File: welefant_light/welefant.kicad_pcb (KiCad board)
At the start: 2 copper layers, 80 x 90 mm, 75 parts, among them J1 Conn_01x02, J2 Conn_02x8_Odd_Even, J3 Conn_02x11_Odd_Even, Q1 AO3401A, Q2 AO3401A, Q3 AO3401A, SW1 RESET, SW2 RESET, SW3 BOOT, U1 NCP167BMX330TBG, U2 Audio Jack PJ-324, U3 GSA4737H12-F26-6P, U4 TP4056, U5 welefant, U6 ESP32-S3-WROOM-1(N16R2)

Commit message: blubb
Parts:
- removed R11: 2.4K, easyeda2kicad:R0603
- added R18: 10K, easyeda2kicad:R0603, F.Cu at (42.0, 50.4)
- added R19: 330, easyeda2kicad:R0603, F.Cu at (50.2, 80.1)
- BT1: value Battery_Cell -> Battery
- D4: value SS34 -> 1N5819WS; footprint easyeda2kicad:SMA_L4.3-W2.6-LS5.2-RD -> Diode_SMD:D_SOD-323
- J1: footprint Connector_JST:JST_PH_B2B-PH-SM4-TB_1x02-1MP_P2.00mm_Vertical -> Connector_JST:JST_PH_B2B-PH-K_1x02_P2.00mm_Vertical
- J2, J3: footprint Connector_PinHeader_2.54mm:PinHeader_2x08_P2.54mm_Vertical_SMD -> hacrafu:PinHeader_2x08_P2.54mm_Vertical_SMD_handsolder
- SW1: value RESET -> DPDT; footprint easyeda2kicad:SW-SMD_4P-L5.1-W5.1-P3.70-LS6.5-TL-2 -> hacrafu:Switch_MSS22D18
- U1: footprint easyeda2kicad:XDFN-4_L1.0-W1.0-P0.65-BL-EP -> hacrafu:XDFN-4
- moved D4 111.2 mm to (96.6, 95.8), turned to 180 degrees
- moved R10 86.2 mm to (55.9, 73.6), turned to -90 degrees
- moved SW1 79.8 mm to (45.9, 86.9), turned to -90 degrees
- moved D2 74.6 mm to (57.8, 59.0), turned to 90 degrees
- moved D1 74.0 mm to (60.0, 59.0), turned to 90 degrees
- moved C8 71.4 mm to (51.5, 74.2), turned to 90 degrees
- moved CLED1 69.8 mm to (50.2, 78.6), turned to 180 degrees
- moved J1 64.5 mm to (46.4, 96.3)
- moved Q2 63.7 mm to (57.9, 78.0), turned to -90 degrees
- moved U4 63.2 mm to (47.5, 74.1), turned to 180 degrees
- moved C11 62.0 mm to (34.0, 46.6), turned to 90 degrees
- moved R9 60.7 mm to (54.6, 79.2), turned to 180 degrees
- moved SW3 57.9 mm to (94.4, 67.0)
- moved D3 57.7 mm to (53.9, 74.4), turned to 90 degrees
- moved C7 56.3 mm to (74.0, 65.9), turned to -90 degrees
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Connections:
- C11 pad 1: Net-(SW2-B) -> /RESET
- C11 pad 2: Net-(SW2-D) -> GND
- C3 pad 1: (no net) -> GND
- C3 pad 2: (no net) -> /V33
- C6 pad 1: (no net) -> /VBUS
- C6 pad 2: (no net) -> GND
- Q1 pad 1: (no net) -> Net-(Q1-G)
- Q1 pad 2: (no net) -> /V33
- Q1 pad 3: (no net) -> /VEXT
- R1 pad 1: (no net) -> /V33
- R1 pad 2: (no net) -> /VEXT_EN
- R17 pad 2: Net-(SW2-B) -> /RESET
- R3 pad 1: (no net) -> Net-(Q1-G)
- R3 pad 2: (no net) -> /VEXT_EN
- SW1 pad 2: Net-(SW1-B) -> unconnected-(SW1-AB1-Pad2)
- SW1 pad 3: /GND -> unconnected-(SW1-B1-Pad3)
- SW1 pad 4: Net-(SW1-D) -> unconnected-(SW1-A2-Pad4)
- SW2 pad 1: unconnected-(SW2-A-Pad1) -> /RESET
- SW2 pad 2: Net-(SW2-B) -> /RESET
- SW2 pad 4: Net-(SW2-D) -> GND
- SW3 pad 1: Net-(SW3-A) -> /IO0
- SW3 pad 2: unconnected-(SW3-B-Pad2) -> /IO0
- SW3 pad 3: unconnected-(SW3-C-Pad3) -> GND
- U1 pad 1: (no net) -> /V33
- U1 pad 2: (no net) -> GND
- U1 pad 3: (no net) -> /VBUS
- U1 pad 4: (no net) -> /VBUS
- U1 pad 5: (no net) -> GND
- U4 pad 9: unconnected-(U4-EP-Pad9) -> GND
- U6 pad 27: Net-(SW3-A) -> /IO0
- U6 pad 3: Net-(SW2-B) -> /RESET
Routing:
- net /VEXT: track 0.00 -> 242.7 mm, vias 0 -> 4
- net /V33: track 0.00 -> 131.2 mm, vias 0 -> 2
- net /TOUCH_T4: track 0.00 -> 115.4 mm, vias 0 -> 3
- net /TOUCH_T1: track 0.00 -> 114.3 mm, vias 0 -> 3
- net /TOUCH_T6: track 0.00 -> 113.0 mm, vias 0 -> 5
- net /TOUCH_T2: track 0.00 -> 108.8 mm, vias 0 -> 3
- net /TOUCH_T5: track 0.00 -> 106.5 mm, vias 0 -> 5
- net /TOUCH_T3: track 0.00 -> 100.3 mm, vias 0 -> 3
- net /USB_DN: track 0.00 -> 97.2 mm
- net /AUDIO_PWM_L: track 0.00 -> 93.6 mm, vias 0 -> 2
- net /USB_DP: track 0.00 -> 88.0 mm
- net /AUDIO_PWM_R: track 0.00 -> 82.2 mm, vias 0 -> 2
- net /V5: track 0.00 -> 81.9 mm, vias 0 -> 2
- net /JACK_SENS: track 0.00 -> 81.0 mm, vias 0 -> 1
- net /LED_MATRIX: track 0.00 -> 70.7 mm, vias 0 -> 8
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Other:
- outline, holes or cut-outs redrawn

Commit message: stand
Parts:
- BT1: footprint hacrafu:LiPo_Recycled -> hacrafu:LiPo_Recycled_welefant
- J3: value Conn_02x11_Odd_Even -> Conn_02x6_Odd_Even; footprint hacrafu:PinHeader_2x08_P2.54mm_Vertical_SMD_handsolder -> hacrafu:PinHeader_2x06_P2.54mm_Vertical_SMD_handsolder
- moved J3 5.09 mm to (94.0, 45.9)
- moved C10 0.22 mm to (43.5, 77.0)
- moved R19 0.08 mm to (50.2, 80.2)
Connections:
- J3 pad 10: /IO36 -> /IO40
- J3 pad 11: /IO37 -> /IO41
- J3 pad 12: /IO38 -> /IO42
- J3 pad 5: /TOUCH_T4 -> /IO35
- J3 pad 6: /TOUCH_T5 -> /IO36
- J3 pad 7: /TOUCH_T6 -> /IO37
- J3 pad 8: /IO21 -> /IO38
- J3 pad 9: /IO35 -> /IO39
- U6 pad 23: /IO21 -> unconnected-(U6-IO21-Pad23)
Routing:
- net GND: track 7.59 -> 61.9 mm, vias 57 -> 100
- net /TOUCH_T4: track 115.4 -> 84.2 mm
- net /TOUCH_T6: track 113.0 -> 82.0 mm, vias 5 -> 3
- net /IO21: track 29.1 -> 0.00 mm, vias 2 -> 0
- net /TOUCH_T5: track 106.5 -> 80.4 mm, vias 5 -> 3
- net /V5: track 81.9 -> 96.3 mm, vias 2 -> 5
- net /LED_MATRIX: track 70.7 -> 84.9 mm, vias 8 -> 6
- net /V33: track 131.2 -> 140.3 mm
- net /TOUCH_T1: track 114.3 -> 105.9 mm
- net /VEXT: track 242.7 -> 248.1 mm
- net /D2_LED: track 32.2 -> 37.4 mm
- net /TOUCH_T2: track 108.8 -> 104.4 mm
- net /TOUCH_ER: track 37.5 -> 41.3 mm, vias 1 -> 3
- net /VBUS: track 60.4 -> 56.8 mm, vias 4 -> 2
- net /VEXT_EN: track 52.0 -> 55.5 mm
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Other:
- board text added: "35"
- board text added: "36"
- board text added: "37"
- board text added: "38"
- board text added: "39"
- board text added: "3V3"
- board text added: "40"
- board text added: "41"
- board text added: "42"
- board text added: "AL"
- board text added: "AR"
- board text added: "BT S E"
- board text added: "BT SENS"
- board text added: "GND"
- board text added: "JCK S"
- board text added: "LED"
- board text added: "LED H"
- board text added: "LED MATRIX"
- board text added: "MIC C"
- board text added: "MIC DATA"
- board text added: "RX"
- board text added: "TX"
- board text added: "U+"
- board text added: "U-"
- board text added: "VEXT"
- board text added: "VEXT EN"
- board text added: "Welefant ${ISSUE_DATE} CC-BY-SA 4.0 HaCraFu e.V. Martin Müllenhaupt https://hacrafu.de/kits"

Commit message: bestellt
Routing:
- net /TOUCH_ER: track 41.3 -> 40.1 mm
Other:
- board text added: "BT SE"
- board text added: "JLCJLCJLCJLC"
- board text removed: "BT S E"

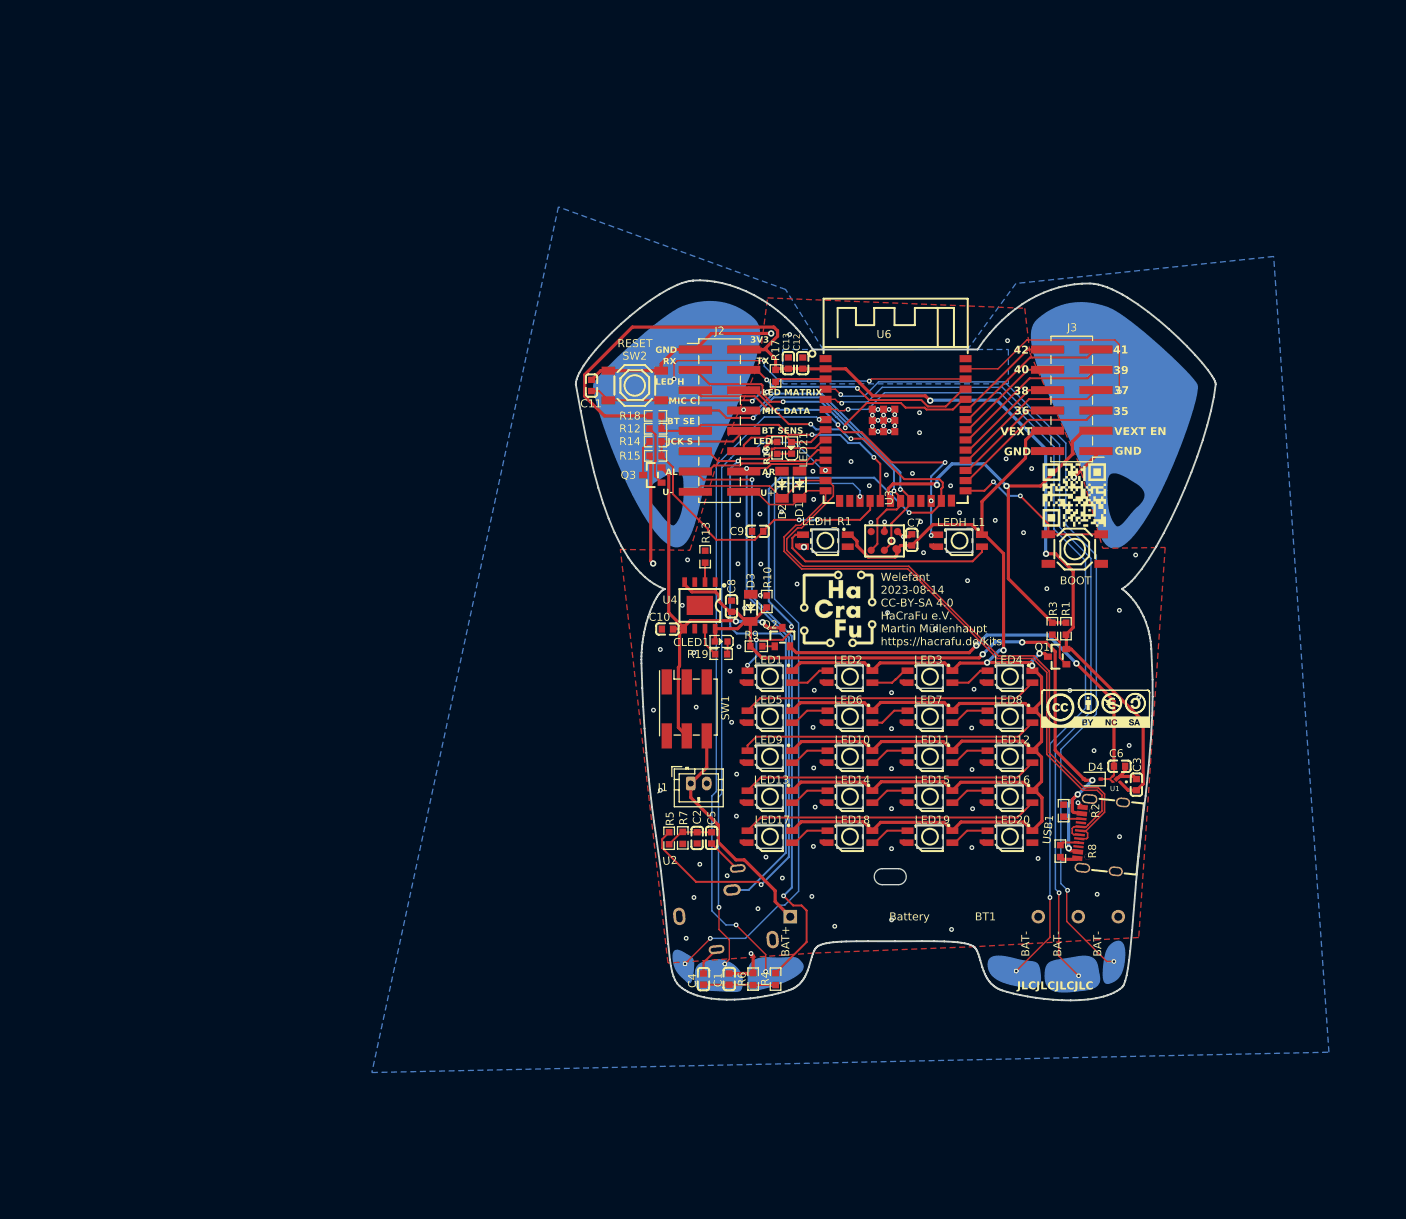
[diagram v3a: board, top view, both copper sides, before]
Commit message: weiter welefant umgestaltung ohne wroom
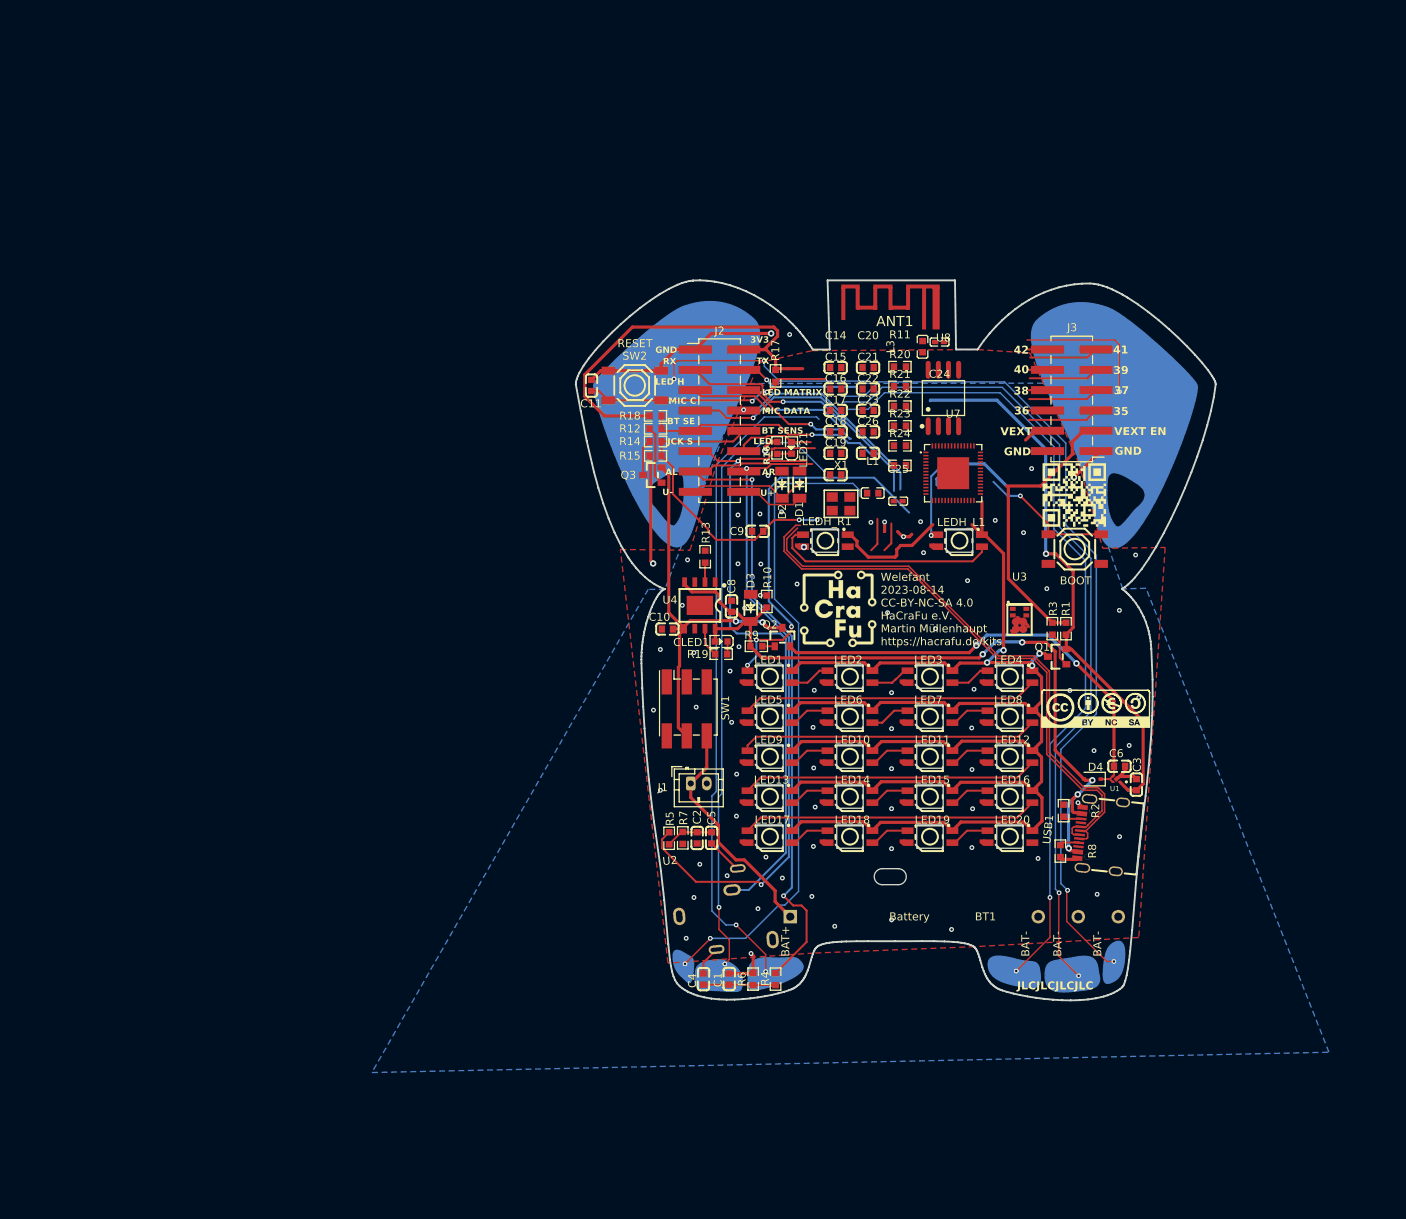
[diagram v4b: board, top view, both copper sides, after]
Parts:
- removed C12, C7: 100n, easyeda2kicad:C0603
- removed C13: 22u, easyeda2kicad:C0603
- removed U6: ESP32-S3-WROOM-1(N16R2), easyeda2kicad:WIRELM-SMD_ESP32-S3-WROOM-1
- added ANT1: ANTENNA, hacrafu:antenna, F.Cu at (71.5, 36.6)
- added C14: 100n, easyeda2kicad:C0603, F.Cu at (64.5, 44.4)
- added C15: 1u, easyeda2kicad:C0603, F.Cu at (64.5, 47.0)
- added C16: 15p, easyeda2kicad:C0603, F.Cu at (64.5, 49.7)
- added C17: 15p, easyeda2kicad:C0603, F.Cu at (64.5, 52.4)
- added C18: 100n, easyeda2kicad:C0603, F.Cu at (64.5, 55.1)
- added C19: 100n, easyeda2kicad:C0603, F.Cu at (64.5, 57.8)
- added C20: 100n, easyeda2kicad:C0603, F.Cu at (68.6, 44.4)
- added C21: 100n, easyeda2kicad:C0603, F.Cu at (68.6, 47.0)
- added C22: 1u, easyeda2kicad:C0603, F.Cu at (68.6, 49.7)
- added C23: 10u, easyeda2kicad:C0603, F.Cu at (68.6, 52.4)
- added C24: 3p3, easyeda2kicad:C0402, F.Cu at (77.5, 41.2)
- added C25: 4p7, easyeda2kicad:C0402, F.Cu at (72.3, 61.1)
- added C26: 100n, easyeda2kicad:C0603, F.Cu at (68.6, 55.1)
- added L1: 2n2, easyeda2kicad:L0603, F.Cu at (69.2, 60.1)
- added L3: 2n2, easyeda2kicad:L0603, F.Cu at (75.4, 41.8)
- added R11: 0, easyeda2kicad:R0603, F.Cu at (72.5, 44.2)
- added R20: 0, easyeda2kicad:R0603, F.Cu at (72.5, 46.7)
- added R21: 0, easyeda2kicad:R0603, F.Cu at (72.5, 49.2)
- added R22: 0, easyeda2kicad:R0603, F.Cu at (72.5, 51.7)
- added R23: 0, easyeda2kicad:R0603, F.Cu at (72.5, 54.1)
- added R24: 0, easyeda2kicad:R0603, F.Cu at (72.5, 56.6)
- added U7: ESP32-S3, easyeda2kicad:QFN-56_L7.0-W7.0-P0.40-TL-EP4.0, F.Cu at (79.2, 57.6)
- added U8: 128MBit Flash, easyeda2kicad:SOIC-8_L5.3-W5.3-P1.27-LS8.0-BL, F.Cu at (78.0, 48.2)
- added X1: 40 MHz, easyeda2kicad:OSC-SMD_4P-L3.2-W2.5-BL_SIT8008BI, F.Cu at (65.2, 61.4)
- U3: value GSA4737H12-F26-6P -> SD18OB261-060; footprint easyeda2kicad:MIC-SMD_GSA4737H12-F26-6P -> easyeda2kicad:MIC-SMD_SD18OB261-060
- moved U3 19.5 mm to (87.5, 75.8), turned to 0 degrees
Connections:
- SW1 pad 4: unconnected-(SW1-A2-Pad4) -> Net-(BT1-+)
- SW1 pad 6: Net-(BT1-+) -> unconnected-(SW1-B2-Pad6)
- SW2 pad 1: /RESET -> unconnected-(SW2-A-Pad1)
- U3 pad 1: GND -> /MIC_DATA
- U3 pad 5: /MIC_DATA -> /VEXT
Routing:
- net /LED_MATRIX: track 84.9 -> 63.9 mm, vias 6 -> 4
- net /V33: track 140.3 -> 122.7 mm, vias 2 -> 1
- net /RX: track 39.9 -> 22.5 mm, vias 2 -> 1
- net /LED_HEAD: track 45.8 -> 30.3 mm, vias 5 -> 2
- net /TX: track 30.5 -> 15.2 mm, vias 2 -> 1
- net /VEXT: track 248.1 -> 233.2 mm
- net /TOUCH_ER: track 40.1 -> 27.9 mm, vias 3 -> 2
- net /USB_DN: track 97.5 -> 85.8 mm
- net /IO41: track 19.8 -> 8.55 mm
- net /IO39: track 19.9 -> 8.73 mm
- net /IO37: track 19.9 -> 8.82 mm
- net /IO38: track 13.4 -> 2.32 mm
- net /IO35: track 19.9 -> 8.88 mm
- net /IO40: track 13.4 -> 2.45 mm
- net /IO36: track 13.4 -> 2.45 mm
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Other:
- outline, holes or cut-outs redrawn
- board text added: "Welefant ${ISSUE_DATE} CC-BY-NC-SA 4.0 HaCraFu e.V. Martin Müllenhaupt https://hacrafu.de/kits"
- board text removed: "Welefant ${ISSUE_DATE} CC-BY-SA 4.0 HaCraFu e.V. Martin Müllenhaupt https://hacrafu.de/kits"

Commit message: weiter
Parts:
- removed C24: 3p3, easyeda2kicad:C0402
- removed C25: 4p7, easyeda2kicad:C0402
- removed C26: 100n, easyeda2kicad:C0603
- removed L3: 2n2, easyeda2kicad:L0603
- added C12: 10u, easyeda2kicad:C0603, F.Cu at (66.3, 45.2)
- added C13: 1u, easyeda2kicad:C0603, F.Cu at (68.0, 45.2)
- added C7: 10u, easyeda2kicad:C0603, F.Cu at (51.9, 79.3)
- added L2: 2n2, easyeda2kicad:L0603, F.Cu at (76.4, 43.9)
- added R25: 0, easyeda2kicad:R0603, F.Cu at (69.8, 57.6)
- added SW4: GPIO33, easyeda2kicad:SW-SMD_4P-L5.1-W5.1-P3.70-LS6.5-TL-2, F.Cu at (103.2, 51.9)
- added SW5: GPIO33, easyeda2kicad:SW-SMD_4P-L5.1-W5.1-P3.70-LS6.5-TL-2, F.Cu at (39.5, 51.9)
- added U6: 128MBit Flash, easyeda2kicad:SOIC-8_L5.3-W5.3-P1.27-LS8.0-BL, F.Cu at (71.9, 64.5)
- C10: value 10u -> 15p
- C11: value 1u -> 15p
- C14: value 100n -> 1u
- C15: value 1u -> 100n
- C16, C17: value 15p -> 100n
- C18: value 100n -> 4p7; footprint easyeda2kicad:C0603 -> easyeda2kicad:C0402
- C19: value 100n -> 3p3; footprint easyeda2kicad:C0603 -> easyeda2kicad:C0402
- C23: value 10u -> 100n
- C3: value 1u -> 10u
- R10: value 10K -> 1K
- R11: value 0 -> 10K
- R12: value 1K -> 330
- R13: value 3K3 -> 10K; footprint easyeda2kicad:R0603_NEW -> easyeda2kicad:R0603
- R14: value 390K -> 1K
- R15: value 100K -> 390K
- R16: value 330 -> 100K
- R17: value 10K -> 3K3; footprint easyeda2kicad:R0603 -> easyeda2kicad:R0603_NEW
- R18: value 10K -> 0
- R19: value 330 -> 10K
- R20: value 0 -> 330
- R9: value 1K -> 100K
- SW1: value DPDT -> ON-OFF; footprint hacrafu:Switch_MSS22D18 -> easyeda2kicad:SW-SMD_MK-12C02-G025
- U1: value NCP167BMX330TBG -> RT9080-33GJ5; footprint hacrafu:XDFN-4 -> easyeda2kicad:TSOT-23-5_L2.9-W1.6-P0.95-LS2.8-BL
- U8: value 128MBit Flash -> Reset 2.8V; footprint easyeda2kicad:SOIC-8_L5.3-W5.3-P1.27-LS8.0-BL -> easyeda2kicad:SOT-23-3_L2.9-W1.6-P1.90-LS2.8-BR
- moved C3 63.7 mm to (44.7, 69.0), turned to 0 degrees
- moved C6 58.9 mm to (44.6, 74.1)
- moved U1 58.5 mm to (46.4, 71.5), turned to 0 degrees
- moved J1 51.7 mm to (97.7, 103.2)
- moved USB1 51.1 mm to (46.6, 98.3), turned to -83 degrees
- moved D4 51.0 mm to (48.1, 79.8), turned to 0 degrees
- moved C11 46.7 mm to (79.8, 56.0), turned to 0 degrees
- moved C10 45.0 mm to (79.7, 50.3)
- moved R8 41.7 mm to (51.0, 103.8), turned to 0 degrees
- moved R2 41.3 mm to (51.8, 101.2), turned to 90 degrees
- moved R18 40.2 mm to (82.1, 53.5), turned to -90 degrees
- moved R19 38.7 mm to (49.1, 41.5), turned to 90 degrees
- moved R11 32.2 mm to (59.3, 73.7), turned to 180 degrees
- moved U8 32.1 mm to (46.6, 41.2), turned to 90 degrees
- moved R17 30.9 mm to (59.4, 76.2), turned to 0 degrees
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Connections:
- BT1 pad 1: Net-(BT1-+) -> /VBAT
- C10 pad 1: GND -> /XTAL_N
- C10 pad 2: /VBAT -> GND
- C11 pad 1: /RESET -> GND
- C11 pad 2: GND -> Net-(X1-OSC2)
- C14 pad 1: GND -> /RESET
- C14 pad 2: /VDD_SPI -> GND
- C15 pad 1: /VDD_SPI -> GND
- C15 pad 2: GND -> /V33
- C16 pad 1: GND -> /V33
- C16 pad 2: Net-(X1-OSC2) -> GND
- C17 pad 1: /XTAL_N -> GND
- C17 pad 2: GND -> Net-(C17-Pad2)
- C18 pad 2: /V33 -> Net-(U7-LNA_IN)
- C19 pad 2: /V33 -> Net-(ANT1-PadFEED)
- C20 pad 2: Net-(C20-Pad2) -> /VDD_SPI
- C22 pad 1: GND -> /VDD_SPI
- C22 pad 2: /V33 -> GND
- C23 pad 1: /V33 -> GND
- C23 pad 2: GND -> /V33
- C6 pad 1: /VBUS -> GND
- C6 pad 2: GND -> /VBUS
- C8 pad 1: /V5 -> GND
- C8 pad 2: GND -> /BAT_SENS
- C9 pad 2: /BAT_SENS -> /VBAT
- D4 pad 1: /VBUS -> Net-(D4-K)
- J1 pad 1: Net-(BT1-+) -> /VBAT
- L1 pad 2: Net-(C20-Pad2) -> Net-(C17-Pad2)
- Q2 pad 2: /VBUS -> Net-(D4-K)
- R10 pad 1: GND -> Net-(Q2-G)
- R11 pad 1: Net-(U7-SPID) -> GND
- R11 pad 2: /SPID -> /V5
- R12 pad 1: Net-(Q3-G) -> Net-(CLED1-C)
- R12 pad 2: /BAT_SENS_EN -> Net-(U4-~{CHRG})
- R13 pad 1: Net-(U4-PROG) -> /V33
- R13 pad 2: GND -> /BAT_SENS_EN
- R14 pad 1: /BAT_SENS -> Net-(Q3-G)
- R14 pad 2: Net-(Q3-D) -> /BAT_SENS_EN
- R15 pad 2: GND -> Net-(Q3-D)
- R16 pad 1: GND -> /BAT_SENS
- R16 pad 2: Net-(LED21-C) -> GND
- R17 pad 1: /V33 -> Net-(U4-PROG)
- R17 pad 2: /RESET -> GND
- R18 pad 1: /V33 -> /XTAL_P
- R18 pad 2: /BAT_SENS_EN -> Net-(X1-OSC2)
- R19 pad 1: Net-(CLED1-C) -> /V33
- R19 pad 2: Net-(U4-~{CHRG}) -> /RESET
- R20 pad 1: Net-(U7-SPIQ) -> GND
- R20 pad 2: /SPIQ -> Net-(LED21-C)
- R21 pad 1: Net-(U7-SPICLK) -> Net-(U7-SPID)
- R21 pad 2: /SPICLK -> /SPID
- R22 pad 1: Net-(U7-SPIWP) -> Net-(U7-SPIQ)
- R22 pad 2: /SPIWP -> /SPIQ
- R23 pad 1: Net-(U7-SPIHD) -> Net-(U7-SPICLK)
- R23 pad 2: /SPIHD -> /SPICLK
- R24 pad 1: /XTAL_P -> Net-(U7-SPIWP)
- R24 pad 2: Net-(X1-OSC2) -> /SPIWP
- R9 pad 1: Net-(Q2-G) -> Net-(U1-EN)
- R9 pad 2: /V5 -> /VBUS
- SW1 pad 1: unconnected-(SW1-A1-Pad1) -> /VBUS
- SW1 pad 2: unconnected-(SW1-AB1-Pad2) -> Net-(D4-K)
- SW1 pad 4: Net-(BT1-+) -> unconnected-(SW1-Pad4)
- SW1 pad 5: /VBAT -> unconnected-(SW1-Pad5)
- SW2 pad 1: unconnected-(SW2-A-Pad1) -> /RESET
- U1 pad 1: /V33 -> /VBUS
- U1 pad 3: /VBUS -> Net-(U1-EN)
- U1 pad 4: /VBUS -> unconnected-(U1-NC-Pad4)
- U1 pad 5: GND -> /V33
- U7 pad 2: Net-(C20-Pad2) -> Net-(C17-Pad2)
- U7 pad 3: Net-(C20-Pad2) -> Net-(C17-Pad2)
- U7 pad 38: unconnected-(U7-GPIO33-Pad38) -> /GPIO33
- U7 pad 39: unconnected-(U7-GPIO34-Pad39) -> /GPIO34
- U8 pad 1: /SPICS0 -> /RESET
- U8 pad 2: /SPIQ -> GND
- U8 pad 3: /SPIWP -> /V33
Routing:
- net /VEXT: track 233.2 -> 0.00 mm, vias 4 -> 0
- net /V33: track 122.7 -> 0.00 mm, vias 1 -> 0
- net /TOUCH_T1: track 103.7 -> 0.00 mm, vias 2 -> 0
- net /TOUCH_T2: track 102.1 -> 0.00 mm, vias 2 -> 0
- net /TOUCH_T3: track 100.1 -> 0.00 mm, vias 2 -> 0
- net /V5: track 96.3 -> 0.00 mm, vias 5 -> 0
- net /AUDIO_PWM_L: track 88.0 -> 0.00 mm, vias 2 -> 0
- net /USB_DN: track 85.8 -> 0.00 mm
- net /TOUCH_T4: track 83.3 -> 0.00 mm, vias 2 -> 0
- net /TOUCH_T6: track 81.4 -> 0.00 mm, vias 2 -> 0
- net /JACK_SENS: track 80.7 -> 0.00 mm, vias 1 -> 0
- net /AUDIO_PWM_R: track 80.7 -> 0.00 mm, vias 2 -> 0
- net /TOUCH_T5: track 80.4 -> 0.00 mm, vias 2 -> 0
- net /USB_DP: track 79.0 -> 0.00 mm
- net /LED_MATRIX: track 63.9 -> 0.00 mm, vias 4 -> 0
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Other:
- outline, holes or cut-outs redrawn
